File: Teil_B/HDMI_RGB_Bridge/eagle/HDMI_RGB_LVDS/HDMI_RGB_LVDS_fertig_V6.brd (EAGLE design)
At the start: 70 x 60 mm, 95 parts, among them CON1 KLDX-0202-A-LT, CON2 FCI-10029449-111RLF, CON3 XF2M-4015-1A, CON4 FCI-10033526-N3212LF, CON5 MOLEX-53261-0671, CON6 FI-X30SSLA-HF, IC2 WPMDL1300331BD, IC4 AT24C01C-SSHM-B, IC5 TFP401APZP, IC6 ATMEGA88PA, IC7 FT232RL, IC8 SN75LVDS83BDGGR, Q1 ATS073ASM-1, T1 IRLML5203TRPBF, T2 IRLML2502TRPBF

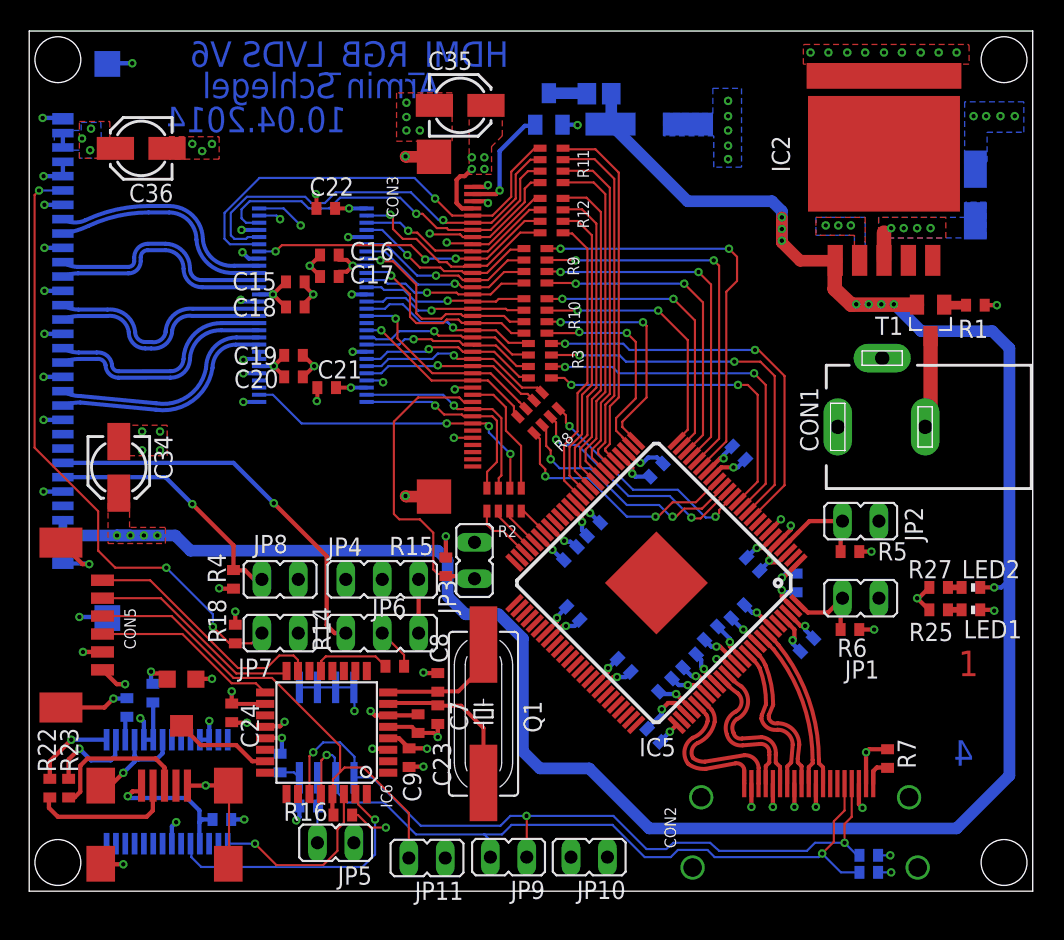
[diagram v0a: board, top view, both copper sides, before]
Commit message: reviewd lbr, changd schematics to V7
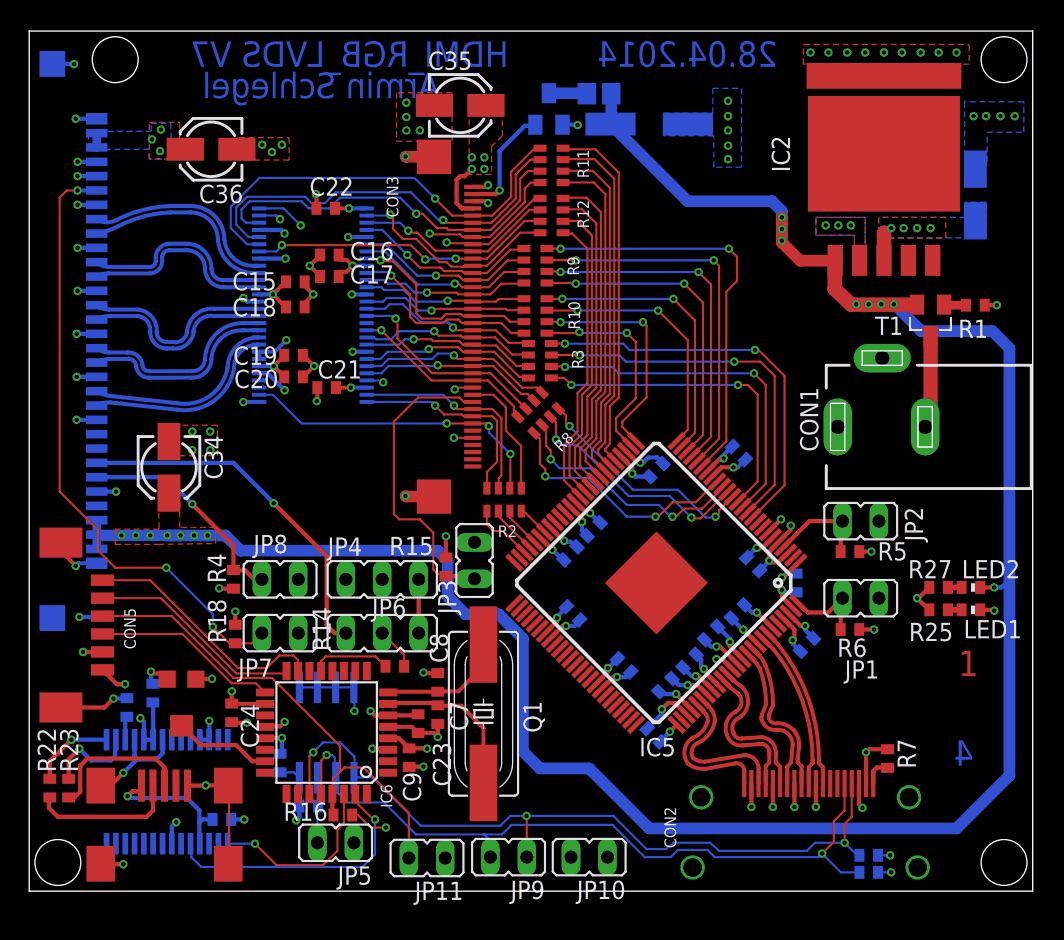
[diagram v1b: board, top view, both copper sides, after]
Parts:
- moved C36 4.88 mm to (12.7, 51.8)
- moved C34 3.50 mm to (9.75, 29.6)
- moved CON6 2.94 mm to (2.06, 38.4), turned to 90 degrees
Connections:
- net +12V: now also CON6.1, CON6.2, CON6.3; no longer CON6.28, CON6.29, CON6.30
- net +3V3: now also CON6.29, CON6.30; no longer CON6.1, CON6.2
- net GND: now also CON6.10, CON6.13, CON6.16, CON6.19, CON6.22, CON6.25, CON6.27, CON6.28, CON6.5; no longer CON6.12, CON6.15, CON6.18, CON6.21, CON6.26, CON6.3, CON6.4, CON6.6, CON6.9
- net LVDS_0_N: now also CON6.24; no longer CON6.7
- net LVDS_0_P: now also CON6.23; no longer CON6.8
- net LVDS_1_N: now also CON6.21; no longer CON6.10
- net LVDS_1_P: now also CON6.20; no longer CON6.11
- net LVDS_2_N: now also CON6.18; no longer CON6.13
- net LVDS_2_P: now also CON6.17; no longer CON6.14
- net LVDS_3_N: now also CON6.12; no longer CON6.19
- net LVDS_3_P: now also CON6.11; no longer CON6.20
- net LVDS_CLK_N: now also CON6.15; no longer CON6.16
- net LVDS_CLK_P: now also CON6.14; no longer CON6.17
- net LVDS_LED_EN: now also CON6.6; no longer CON6.25
- net LVDS_PWM: now also CON6.7; no longer CON6.24
- net LVDS_REVSCAN: now also CON6.26; no longer CON6.5
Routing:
- net GND: track 153.3 -> 156.6 mm, vias 104 -> 105
- net +12V: track 164.4 -> 161.9 mm, vias 12 -> 15
- net LVDS_PWM: track 27.5 -> 25.1 mm
- net LVDS_LED_EN: track 17.8 -> 15.5 mm
- net LVDS_1_P: track 15.6 -> 13.3 mm
- net LVDS_CLK_P: track 15.5 -> 13.1 mm
- net LVDS_3_P: track 15.4 -> 13.0 mm
- net LVDS_CLK_N: track 15.5 -> 13.2 mm
- net LVDS_1_N: track 15.6 -> 13.3 mm
- net LVDS_3_N: track 15.4 -> 13.1 mm
- net LVDS_0_N: track 15.4 -> 13.1 mm
- net LVDS_0_P: track 15.5 -> 13.2 mm
- net LVDS_2_P: track 15.4 -> 13.2 mm
- net LVDS_2_N: track 15.4 -> 13.3 mm
- net RGB_EVEN_R1: track 29.9 -> 28.8 mm
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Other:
- board text added: "28.04.2014"
- board text added: "HDMI_RGB_LVDS V7"
- board text removed: "10.04.2014"
- board text removed: "HDMI_RGB_LVDS V6"
